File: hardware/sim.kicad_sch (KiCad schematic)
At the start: 11 parts, among them J12 Conn_01x06, J13 SIM_Card

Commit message: HW: Update BOM
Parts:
- J12: value Conn_01x06 -> PRPC006SAAN-RC
- J13: value SIM_Card -> SIM8070-6-0-11-00-A
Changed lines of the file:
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@@
 			)
 		)
-		(property "Value" "Conn_01x06"
+		(property "Value" "PRPC006SAAN-RC"
 			(at 83.566 108.712 0)
 			(effects
@@
 			)
 		)
-		(property "Value" "SIM_Card"
+		(property "Value" "SIM8070-6-0-11-00-A"
 			(at 204.47 116.84 0)
 			(effects

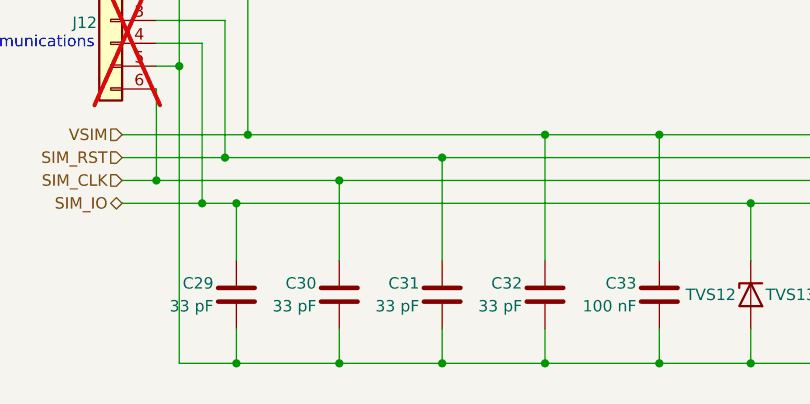
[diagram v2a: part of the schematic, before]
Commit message: HW: Connect +BATT to MCU
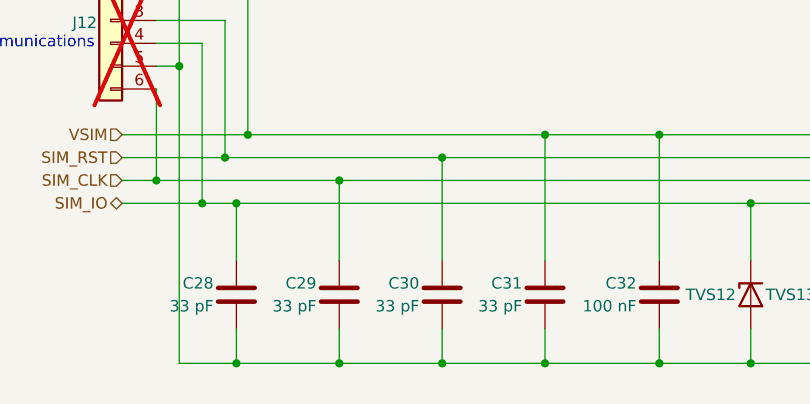
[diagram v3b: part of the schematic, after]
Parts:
- renumbered C29 to C28, C30 to C29, C31 to C30, C32 to C31, C33 to C32
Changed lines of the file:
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@@
 	(title_block
 		(title "Iida devkit")
-		(date "2024-09-22")
-		(rev "v4.1.0")
+		(date "2024-09-25")
+		(rev "v4.2.0")
 	)
 	(junction
@@
 		(on_board yes)
 		(dnp no)
-		(property "Reference" "C33"
+		(property "Reference" "C32"
 			(at 143.51 135.89 0)
 			(effects
@@
 			(project "iida_devkit"
 				(path "/b12a6e25-97fb-4aba-bc96-af8db389bb9a/33580d9f-a609-4568-baaf-9a29cf2dabcd"
-					(reference "C33")
+					(reference "C32")
 					(unit 1)
 				)
@@
 		(on_board yes)
 		(dnp no)
-		(property "Reference" "C30"
+		(property "Reference" "C29"
 			(at 107.95 135.89 0)
 			(effects
@@
 			(project "iida_devkit"
 				(path "/b12a6e25-97fb-4aba-bc96-af8db389bb9a/33580d9f-a609-4568-baaf-9a29cf2dabcd"
-					(reference "C30")
+					(reference "C29")
 					(unit 1)
 				)
@@
 		(on_board yes)
 		(dnp no)
-		(property "Reference" "C29"
+		(property "Reference" "C28"
 			(at 96.52 135.89 0)
 			(effects
@@
 			(project "iida_devkit"
 				(path "/b12a6e25-97fb-4aba-bc96-af8db389bb9a/33580d9f-a609-4568-baaf-9a29cf2dabcd"
-					(reference "C29")
+					(reference "C28")
 					(unit 1)
 				)
@@
 		(on_board yes)
 		(dnp no)
-		(property "Reference" "C31"
+		(property "Reference" "C30"
 			(at 119.38 135.89 0)
 			(effects
@@
 			(project "iida_devkit"
 				(path "/b12a6e25-97fb-4aba-bc96-af8db389bb9a/33580d9f-a609-4568-baaf-9a29cf2dabcd"
-					(reference "C31")
+					(reference "C30")
 					(unit 1)
 				)
@@
 		(on_board yes)
 		(dnp no)
-		(property "Reference" "C32"
+		(property "Reference" "C31"
 			(at 130.81 135.89 0)
 			(effects
@@
 			(project "iida_devkit"
 				(path "/b12a6e25-97fb-4aba-bc96-af8db389bb9a/33580d9f-a609-4568-baaf-9a29cf2dabcd"
-					(reference "C32")
+					(reference "C31")
 					(unit 1)
 				)

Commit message: HW: Update components
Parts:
- C28, C29, C30, C31: Digi-Key Part Number 490-5936-1-ND -> 732-7472-1-ND; Manufacturer Murata Electronics -> Würth Elektronik; Manufacturer Part Number GRM1555C1H330JA01D -> 885012005058
- C32: Digi-Key Part Number 490-7998-1-ND -> 732-7513-1-ND; Manufacturer Murata Electronics -> Würth Elektronik; Manufacturer Part Number GCM155R71C104KA55J -> 885012205018
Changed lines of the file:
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@@
 			)
 		)
-		(property "Manufacturer" "Murata Electronics"
+		(property "Manufacturer" "Würth Elektronik"
 			(at 146.05 137.16 0)
 			(effects
@@
 			)
 		)
-		(property "Manufacturer Part Number" "GCM155R71C104KA55J"
+		(property "Manufacturer Part Number" "885012205018"
 			(at 146.05 137.16 0)
 			(effects
@@
 			)
 		)
-		(property "Digi-Key Part Number" "490-7998-1-ND"
+		(property "Digi-Key Part Number" "732-7513-1-ND"
 			(at 146.05 137.16 0)
 			(effects
@@
 			)
 		)
-		(property "Digi-Key Part Number" "490-5936-1-ND"
+		(property "Digi-Key Part Number" "732-7472-1-ND"
 			(at 110.49 137.16 0)
 			(effects
@@
 			)
 		)
-		(property "Manufacturer" "Murata Electronics"
+		(property "Manufacturer" "Würth Elektronik"
 			(at 110.49 137.16 0)
 			(effects
@@
 			)
 		)
-		(property "Manufacturer Part Number" "GRM1555C1H330JA01D"
+		(property "Manufacturer Part Number" "885012005058"
 			(at 110.49 137.16 0)
 			(effects
@@
 			)
 		)
-		(property "Digi-Key Part Number" "490-5936-1-ND"
+		(property "Digi-Key Part Number" "732-7472-1-ND"
 			(at 99.06 137.16 0)
 			(effects
@@
 			)
 		)
-		(property "Manufacturer" "Murata Electronics"
+		(property "Manufacturer" "Würth Elektronik"
 			(at 99.06 137.16 0)
 			(effects
@@
 			)
 		)
-		(property "Manufacturer Part Number" "GRM1555C1H330JA01D"
+		(property "Manufacturer Part Number" "885012005058"
 			(at 99.06 137.16 0)
 			(effects
@@
 			)
 		)
-		(property "Digi-Key Part Number" "490-5936-1-ND"
+		(property "Digi-Key Part Number" "732-7472-1-ND"
 			(at 121.92 137.16 0)
 			(effects
@@
 			)
 		)
-		(property "Manufacturer" "Murata Electronics"
+		(property "Manufacturer" "Würth Elektronik"
 			(at 121.92 137.16 0)
 			(effects
@@
 			)
 		)
-		(property "Manufacturer Part Number" "GRM1555C1H330JA01D"
+		(property "Manufacturer Part Number" "885012005058"
 			(at 121.92 137.16 0)
 			(effects
@@
 			)
 		)
-		(property "Digi-Key Part Number" "490-5936-1-ND"
+		(property "Digi-Key Part Number" "732-7472-1-ND"
 			(at 133.35 137.16 0)
 			(effects
@@
 			)
 		)
-		(property "Manufacturer" "Murata Electronics"
+		(property "Manufacturer" "Würth Elektronik"
 			(at 133.35 137.16 0)
 			(effects
@@
 			)
 		)
-		(property "Manufacturer Part Number" "GRM1555C1H330JA01D"
+		(property "Manufacturer Part Number" "885012005058"
 			(at 133.35 137.16 0)
 			(effects

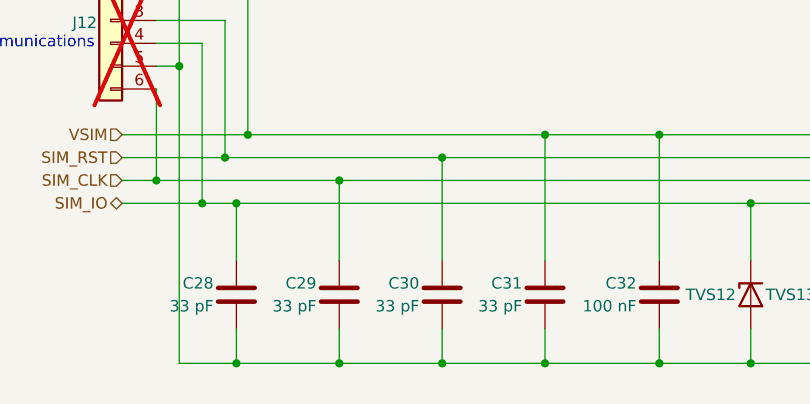
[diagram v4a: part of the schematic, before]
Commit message: HW: Start adding Li-Po support
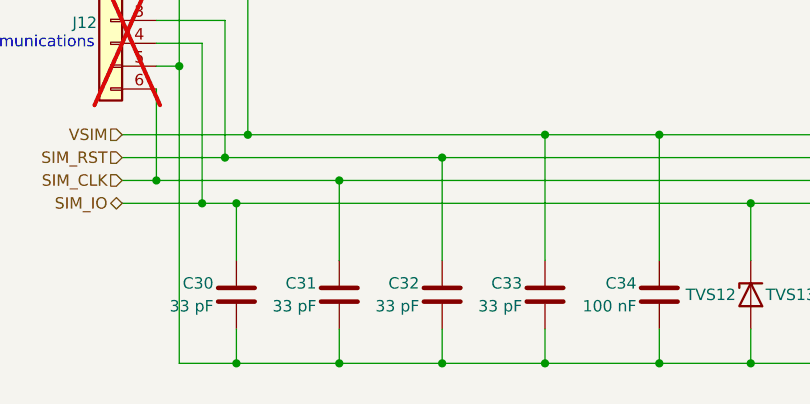
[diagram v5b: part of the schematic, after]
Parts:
- renumbered C28 to C30, C29 to C31, C30 to C32, C31 to C33, C32 to C34
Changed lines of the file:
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@@
 		(on_board yes)
 		(dnp no)
-		(property "Reference" "C32"
+		(property "Reference" "C34"
 			(at 143.51 135.89 0)
 			(effects
@@
 			(project "iida_devkit"
 				(path "/b12a6e25-97fb-4aba-bc96-af8db389bb9a/33580d9f-a609-4568-baaf-9a29cf2dabcd"
-					(reference "C32")
+					(reference "C34")
 					(unit 1)
 				)
@@
 		(on_board yes)
 		(dnp no)
-		(property "Reference" "C29"
+		(property "Reference" "C31"
 			(at 107.95 135.89 0)
 			(effects
@@
 			(project "iida_devkit"
 				(path "/b12a6e25-97fb-4aba-bc96-af8db389bb9a/33580d9f-a609-4568-baaf-9a29cf2dabcd"
-					(reference "C29")
+					(reference "C31")
 					(unit 1)
 				)
@@
 		(on_board yes)
 		(dnp no)
-		(property "Reference" "C28"
+		(property "Reference" "C30"
 			(at 96.52 135.89 0)
 			(effects
@@
 			(project "iida_devkit"
 				(path "/b12a6e25-97fb-4aba-bc96-af8db389bb9a/33580d9f-a609-4568-baaf-9a29cf2dabcd"
-					(reference "C28")
+					(reference "C30")
 					(unit 1)
 				)
@@
 		(on_board yes)
 		(dnp no)
-		(property "Reference" "C30"
+		(property "Reference" "C32"
 			(at 119.38 135.89 0)
 			(effects
@@
 			(project "iida_devkit"
 				(path "/b12a6e25-97fb-4aba-bc96-af8db389bb9a/33580d9f-a609-4568-baaf-9a29cf2dabcd"
-					(reference "C30")
+					(reference "C32")
 					(unit 1)
 				)
@@
 		(dnp no)
 		(fields_autoplaced yes)
-		(property "Reference" "#PWR027"
+		(property "Reference" "#PWR049"
 			(at 187.96 151.13 0)
 			(effects
@@
 			(project "iida_devkit"
 				(path "/b12a6e25-97fb-4aba-bc96-af8db389bb9a/33580d9f-a609-4568-baaf-9a29cf2dabcd"
-					(reference "#PWR027")
+					(reference "#PWR049")
 					(unit 1)
 				)
@@
 		(on_board yes)
 		(dnp no)
-		(property "Reference" "C31"
+		(property "Reference" "C33"
 			(at 130.81 135.89 0)
 			(effects
@@
 			(project "iida_devkit"
 				(path "/b12a6e25-97fb-4aba-bc96-af8db389bb9a/33580d9f-a609-4568-baaf-9a29cf2dabcd"
-					(reference "C31")
-					(unit 1)
-				)
+					(reference "C33")
+					(unit 1)
+				)

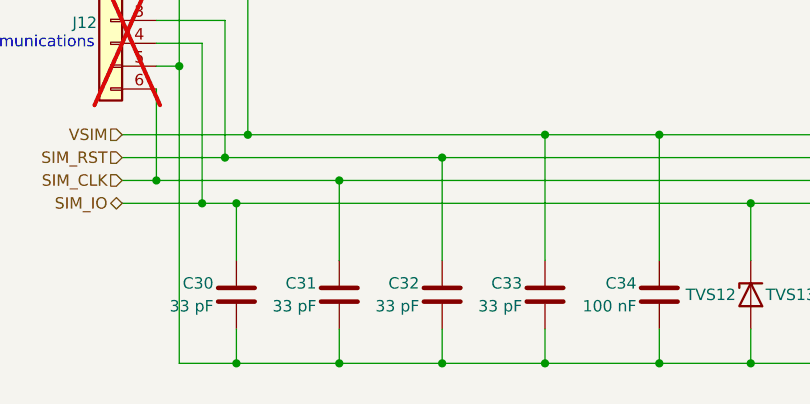
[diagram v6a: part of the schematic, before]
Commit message: HW: Update components to be hand solderable
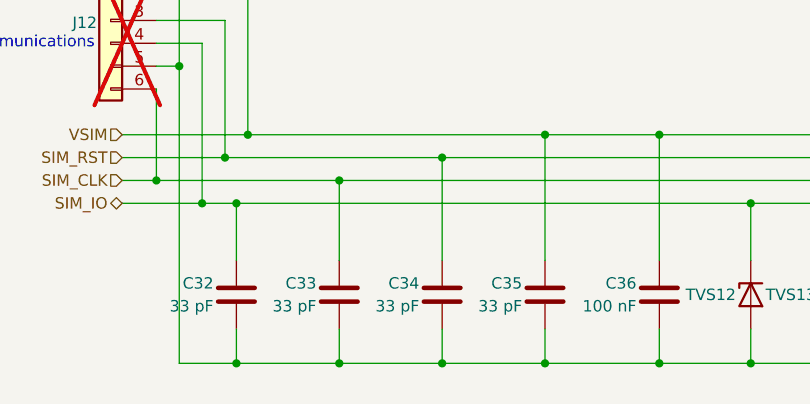
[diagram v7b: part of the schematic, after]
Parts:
- C32: renamed from C30; footprint perfect_footprints:0402_1005_perfect -> Capacitor_SMD:C_0402_1005Metric_Pad0.74x0.62mm_HandSolder
- C33: renamed from C31; footprint perfect_footprints:0402_1005_perfect -> Capacitor_SMD:C_0402_1005Metric_Pad0.74x0.62mm_HandSolder
- C34: renamed from C32; footprint perfect_footprints:0402_1005_perfect -> Capacitor_SMD:C_0402_1005Metric_Pad0.74x0.62mm_HandSolder
- C35: renamed from C33; footprint perfect_footprints:0402_1005_perfect -> Capacitor_SMD:C_0402_1005Metric_Pad0.74x0.62mm_HandSolder
- C36: renamed from C34; footprint perfect_footprints:0402_1005_perfect -> Capacitor_SMD:C_0402_1005Metric_Pad0.74x0.62mm_HandSolder
- TVS12, TVS13, TVS14, TVS15: footprint perfect_footprints:0402_1005_perfect -> Diode_SMD:D_0402_1005Metric_Pad0.77x0.64mm_HandSolder
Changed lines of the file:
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@@
 		(on_board yes)
 		(dnp no)
-		(property "Reference" "C34"
+		(property "Reference" "C36"
 			(at 143.51 135.89 0)
 			(effects
@@
 			)
 		)
-		(property "Footprint" "perfect_footprints:0402_1005_perfect"
+		(property "Footprint" "Capacitor_SMD:C_0402_1005Metric_Pad0.74x0.62mm_HandSolder"
 			(at 145.0848 140.97 0)
 			(effects
@@
 			(project "iida_devkit"
 				(path "/b12a6e25-97fb-4aba-bc96-af8db389bb9a/33580d9f-a609-4568-baaf-9a29cf2dabcd"
-					(reference "C34")
+					(reference "C36")
 					(unit 1)
 				)
@@
 			)
 		)
-		(property "Footprint" "perfect_footprints:0402_1005_perfect"
+		(property "Footprint" "Diode_SMD:D_0402_1005Metric_Pad0.77x0.64mm_HandSolder"
 			(at 165.1 137.16 0)
 			(effects
@@
 		(on_board yes)
 		(dnp no)
-		(property "Reference" "C31"
+		(property "Reference" "C33"
 			(at 107.95 135.89 0)
 			(effects
@@
 			)
 		)
-		(property "Footprint" "perfect_footprints:0402_1005_perfect"
+		(property "Footprint" "Capacitor_SMD:C_0402_1005Metric_Pad0.74x0.62mm_HandSolder"
 			(at 111.4552 140.97 0)
 			(effects
@@
 			(project "iida_devkit"
 				(path "/b12a6e25-97fb-4aba-bc96-af8db389bb9a/33580d9f-a609-4568-baaf-9a29cf2dabcd"
-					(reference "C31")
+					(reference "C33")
 					(unit 1)
 				)
@@
 		(on_board yes)
 		(dnp no)
-		(property "Reference" "C30"
+		(property "Reference" "C32"
 			(at 96.52 135.89 0)
 			(effects
@@
 			)
 		)
-		(property "Footprint" "perfect_footprints:0402_1005_perfect"
+		(property "Footprint" "Capacitor_SMD:C_0402_1005Metric_Pad0.74x0.62mm_HandSolder"
 			(at 100.0252 140.97 0)
 			(effects
@@
 			(project "iida_devkit"
 				(path "/b12a6e25-97fb-4aba-bc96-af8db389bb9a/33580d9f-a609-4568-baaf-9a29cf2dabcd"
-					(reference "C30")
+					(reference "C32")
 					(unit 1)
 				)
@@
 			)
 		)
-		(property "Footprint" "perfect_footprints:0402_1005_perfect"
+		(property "Footprint" "Diode_SMD:D_0402_1005Metric_Pad0.77x0.64mm_HandSolder"
 			(at 182.88 137.16 0)
 			(effects
@@
 			)
 		)
-		(property "Footprint" "perfect_footprints:0402_1005_perfect"
+		(property "Footprint" "Diode_SMD:D_0402_1005Metric_Pad0.77x0.64mm_HandSolder"
 			(at 156.21 137.16 0)
 			(effects
@@
 		(on_board yes)
 		(dnp no)
-		(property "Reference" "C32"
+		(property "Reference" "C34"
 			(at 119.38 135.89 0)
 			(effects
@@
 			)
 		)
-		(property "Footprint" "perfect_footprints:0402_1005_perfect"
+		(property "Footprint" "Capacitor_SMD:C_0402_1005Metric_Pad0.74x0.62mm_HandSolder"
 			(at 122.8852 140.97 0)
 			(effects
@@
 			(project "iida_devkit"
 				(path "/b12a6e25-97fb-4aba-bc96-af8db389bb9a/33580d9f-a609-4568-baaf-9a29cf2dabcd"
-					(reference "C32")
+					(reference "C34")
 					(unit 1)
 				)
@@
 			)
 		)
-		(property "Footprint" "perfect_footprints:0402_1005_perfect"
+		(property "Footprint" "Diode_SMD:D_0402_1005Metric_Pad0.77x0.64mm_HandSolder"
 			(at 173.99 137.16 0)
 			(effects
@@
 		(dnp no)
 		(fields_autoplaced yes)
-		(property "Reference" "#PWR052"
+		(property "Reference" "#PWR058"
 			(at 187.96 151.13 0)
 			(effects
@@
 			(project "iida_devkit"
 				(path "/b12a6e25-97fb-4aba-bc96-af8db389bb9a/33580d9f-a609-4568-baaf-9a29cf2dabcd"
-					(reference "#PWR052")
+					(reference "#PWR058")
 					(unit 1)
 				)
@@
 		(on_board yes)
 		(dnp no)
-		(property "Reference" "C33"
+		(property "Reference" "C35"
 			(at 130.81 135.89 0)
 			(effects
@@
 			)
 		)
-		(property "Footprint" "perfect_footprints:0402_1005_perfect"
+		(property "Footprint" "Capacitor_SMD:C_0402_1005Metric_Pad0.74x0.62mm_HandSolder"
 			(at 134.3152 140.97 0)
 			(effects
@@
 			(project "iida_devkit"
 				(path "/b12a6e25-97fb-4aba-bc96-af8db389bb9a/33580d9f-a609-4568-baaf-9a29cf2dabcd"
-					(reference "C33")
-					(unit 1)
-				)
+					(reference "C35")
+					(unit 1)
+				)
